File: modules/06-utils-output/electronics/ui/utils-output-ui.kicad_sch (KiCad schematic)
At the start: 33 parts, among them J1 Conn_02x03_Odd_Even, J2 Conn_02x04_Odd_Even, J4 Conn_01x02, J5 Conn_01x06, J6 Conn_02x05_Odd_Even, J7 Conn_02x03_Odd_Even, Q1 2N3904, Q2 2N3906

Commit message: Added Utils BOM
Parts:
- J2: Part URL (none) -> https://mou.sr/4qqxl75; Part no. (none) -> 200-SSW10401TD; Vendor (none) -> Mouser
- J6: Part URL (none) -> https://mou.sr/4lVCZM9; Part no. (none) -> 200-SSW10501TD; Vendor (none) -> Mouser
- J7: Part URL (none) -> https://mou.sr/3GIDVEr; Part no. (none) -> 200-SSW10301TD; Vendor (none) -> Mouser
- Q1: Part URL (none) -> https://mou.sr/4febysZ; Part no. (none) -> 637-2N3904; Vendor (none) -> Mouser
- Q2: Part URL (none) -> https://mou.sr/4a8lju1; Part no. (none) -> 637-2N3906; Vendor (none) -> Mouser
- R1: Part URL (none) -> https://mou.sr/3MWzgkZ; Part no. (none) -> 603-MFR-25FRF52-47K; Vendor (none) -> Mouser
- R2: Part URL (none) -> https://mou.sr/4q072Ei; Part no. (none) -> 603-MFR25SFTF52-4K7; Vendor (none) -> Mouser
- RV_LFO_AMOUNT1: Part no. (none) -> 652-PTV1124425AA203; Vendor (none) -> Mouser
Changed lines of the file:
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@@
 			)
 		)
-		(property "Part URL" ""
+		(property "Part URL" "https://mou.sr/3GIDVEr"
 			(at 245.11 81.28 0)
 			(effects
@@
 			)
 		)
-		(property "Vendor" ""
+		(property "Vendor" "Mouser"
 			(at 245.11 81.28 0)
 			(effects
@@
 			)
 		)
+		(property "Part no." "200-SSW10301TD"
+			(at 245.11 81.28 0)
+			(effects
+				(font
+					(size 1.27 1.27)
+				)
+				(hide yes)
+			)
+		)
 		(pin "3"
 		)
@@
 			)
 		)
-		(property "Vendor" ""
+		(property "Vendor" "Mouser"
 			(at 135.89 55.88 0)
 			(effects
@@
 			)
 		)
+		(property "Part no." "652-PTV1124425AA203 "
+			(at 135.89 55.88 0)
+			(effects
+				(font
+					(size 1.27 1.27)
+				)
+				(hide yes)
+			)
+		)
 		(pin "1"
 		)
@@
 			)
 		)
-		(property "Part URL" ""
+		(property "Part URL" "https://mou.sr/4qqxl75"
 			(at 245.11 60.96 0)
 			(effects
@@
 			)
 		)
-		(property "Vendor" ""
+		(property "Vendor" "Mouser"
 			(at 245.11 60.96 0)
 			(effects
@@
 			)
 		)
+		(property "Part no." "200-SSW10401TD"
+			(at 245.11 60.96 0)
+			(effects
+				(font
+					(size 1.27 1.27)
+				)
+				(hide yes)
+			)
+		)
 		(pin "5"
 		)
@@
 			)
 		)
-		(property "Part URL" ""
+		(property "Part URL" "https://mou.sr/4a8lju1"
 			(at 102.87 179.07 0)
 			(effects
@@
 			)
 		)
-		(property "Vendor" ""
+		(property "Vendor" "Mouser"
 			(at 102.87 179.07 0)
 			(effects
@@
 			)
 		)
+		(property "Part no." "637-2N3906"
+			(at 102.87 179.07 0)
+			(effects
+				(font
+					(size 1.27 1.27)
+				)
+				(hide yes)
+			)
+		)
 		(pin "1"
 		)
@@
 			)
 		)
-		(property "Vendor" ""
+		(property "Vendor" "Mouser"
 			(at 105.41 55.88 0)
 			(effects
@@
 			)
 		)
+		(property "Part no." "652-PTV1124425AA203 "
+			(at 105.41 55.88 0)
+			(effects
+				(font
+					(size 1.27 1.27)
+				)
+				(hide yes)
+			)
+		)
 		(pin "1"
 		)
@@
 			)
 		)
-		(property "Part URL" ""
+		(property "Part URL" "https://mou.sr/4febysZ"
 			(at 102.87 156.21 0)
 			(effects
@@
 			)
 		)
-		(property "Vendor" ""
+		(property "Vendor" "Mouser"
 			(at 102.87 156.21 0)
 			(effects
@@
 			)
 		)
+		(property "Part no." "637-2N3904"
+			(at 102.87 156.21 0)
+			(effects
+				(font
+					(size 1.27 1.27)
+				)
+				(hide yes)
+			)
+		)
 		(pin "2"
 		)
@@
 			)
 		)
-		(property "Part URL" ""
+		(property "Part URL" "https://mou.sr/3MWzgkZ"
 			(at 90.17 156.21 0)
 			(effects
@@
 			)
 		)
-		(property "Vendor" ""
+		(property "Vendor" "Mouser"
 			(at 90.17 156.21 0)
 			(effects
@@
 			)
 		)
+		(property "Part no." "603-MFR-25FRF52-47K"
+			(at 90.17 156.21 90)
+			(effects
+				(font
+					(size 1.27 1.27)
+				)
+				(hide yes)
+			)
+		)
 		(pin "1"
 		)
@@
 			)
 		)
-		(property "Part URL" ""
+		(property "Part URL" "https://mou.sr/4lVCZM9"
 			(at 245.11 100.33 0)
 			(effects
@@
 			)
 		)
-		(property "Vendor" ""
+		(property "Vendor" "Mouser"
 			(at 245.11 100.33 0)
 			(effects
@@
 			)
 		)
+		(property "Part no." "200-SSW10501TD"
+			(at 245.11 100.33 0)
+			(effects
+				(font
+					(size 1.27 1.27)
+				)
+				(hide yes)
+			)
+		)
 		(pin "1"
 		)
@@
 			)
 		)
-		(property "Part URL" ""
+		(property "Part URL" "https://mou.sr/4q072Ei"
 			(at 105.41 146.05 0)
 			(effects
@@
 			)
 		)
-		(property "Vendor" ""
+		(property "Vendor" "Mouser"
 			(at 105.41 146.05 0)
 			(effects
@@
 			(at 105.41 146.05 0)
 			(effects
+				(font
+					(size 1.27 1.27)
+				)
+				(hide yes)
+			)
+		)
+		(property "Part no." "603-MFR25SFTF52-4K7"
+			(at 105.41 146.05 0)
+			(effects

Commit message: Fixed UI component part number bugs
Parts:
- RV_CRUSH1: Part URL https://mou.sr/4694GMU -> https://mou.sr/3VpxrOs; Part no. 652-PTV09A4025FB104 -> 652-PTV09A4025FA105
- RV_LFO_RATE1: value A500k -> A500k-1M; Part URL https://mou.sr/4694GMU -> https://mou.sr/3VpxrOs; Part no. 652-PTV09A4025FB104 -> 652-PTV09A4025FA105
- RV_MAIN_VOLUME1: Part URL https://mou.sr/4694GMU -> https://mou.sr/4bCOV0e; Part no. 652-PTV09A4025FB104 -> 652-PTV09A4025FA103
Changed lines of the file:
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@@
 			)
 		)
-		(property "Part URL" "https://mou.sr/4694GMU"
+		(property "Part URL" "https://mou.sr/4bCOV0e"
 			(at 171.45 29.21 0)
 			(effects
@@
 			)
 		)
-		(property "Part no." "652-PTV09A4025FB104"
+		(property "Part no." "652-PTV09A4025FA103"
 			(at 171.45 29.21 0)
 			(effects
@@
 			)
 		)
-		(property "Part URL" "https://mou.sr/4694GMU"
+		(property "Part URL" "https://mou.sr/3VpxrOs"
 			(at 34.29 29.21 0)
 			(effects
@@
 			)
 		)
-		(property "Part no." "652-PTV09A4025FB104"
+		(property "Part no." "652-PTV09A4025FA105"
 			(at 34.29 29.21 0)
 			(effects
@@
 			)
 		)
-		(property "Value" "A500k"
+		(property "Value" "A500k-1M"
 			(at 102.87 27.9401 0)
 			(effects
@@
 			)
 		)
-		(property "Part URL" "https://mou.sr/4694GMU"
+		(property "Part URL" "https://mou.sr/3VpxrOs"
 			(at 105.41 29.21 0)
 			(effects
@@
 			)
 		)
-		(property "Part no." "652-PTV09A4025FB104"
+		(property "Part no." "652-PTV09A4025FA105"
 			(at 105.41 29.21 0)
 			(effects

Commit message: Updated UI BOMs
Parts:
- RV_CRUSH1, RV_LFO_AMOUNT1, RV_LFO_RATE1, RV_MAIN_VOLUME1: Note (none) -> D-Shaft
- RV_DRIVE1: Note (none) -> Knurled Shaft; Part URL https://mou.sr/4694GMU -> https://mou.sr/41lYe2k; Part no. 652-PTV09A4025FB104 -> 652-PTV09A4025UB104

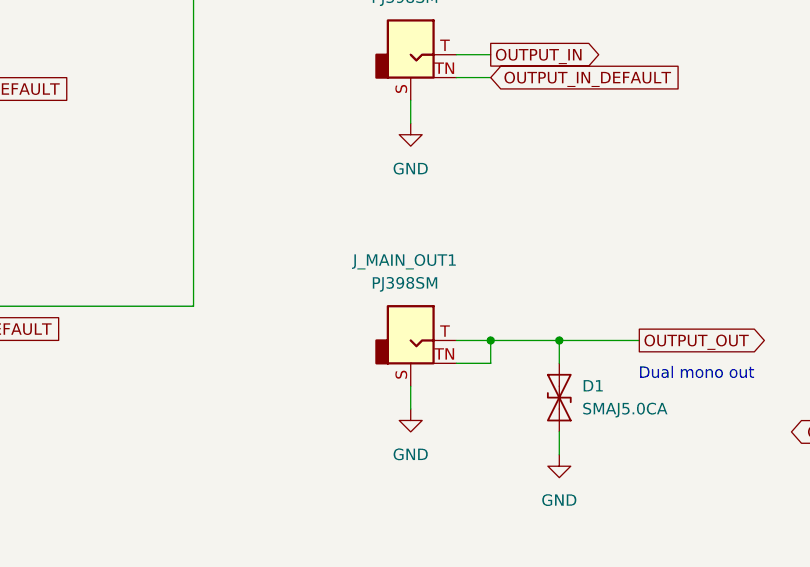
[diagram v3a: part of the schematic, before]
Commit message: Updated main output jack part no
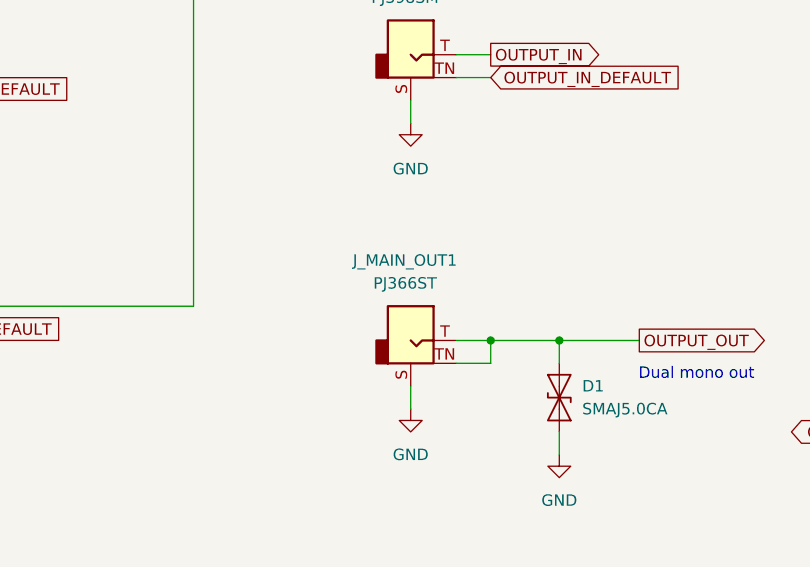
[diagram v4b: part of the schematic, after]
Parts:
- J_MAIN_OUT1: value PJ398SM -> PJ366ST; Note (none) -> Stereo jack; Part URL https://www.thonk.co.uk/shop/thonkiconn/ -> https://www.thonk.co.uk/shop/3-5mm-jacks/; Part no. PJ398SM -> PJ366ST
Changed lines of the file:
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@@
 			)
 		)
-		(property "Value" "PJ398SM"
+		(property "Value" "PJ366ST"
 			(at 170.815 109.22 0)
 			(effects
@@
 			)
 		)
-		(property "Part URL" "https://www.thonk.co.uk/shop/thonkiconn/"
+		(property "Part URL" "https://www.thonk.co.uk/shop/3-5mm-jacks/"
 			(at 171.45 115.57 0)
 			(effects
@@
 			)
 		)
-		(property "Part no." "PJ398SM"
+		(property "Part no." "PJ366ST"
 			(at 171.45 115.57 0)
 			(effects
@@
 			)
 		)
-		(property "Note" ""
+		(property "Note" "Stereo jack"
 			(at 171.45 115.57 0)
 			(effects
+				(font
+					(size 1.27 1.27)
+				)
+				(hide yes)
+			)
+		)
+		(property "Part No." ""
+			(at 171.45 115.57 0)
+			(effects

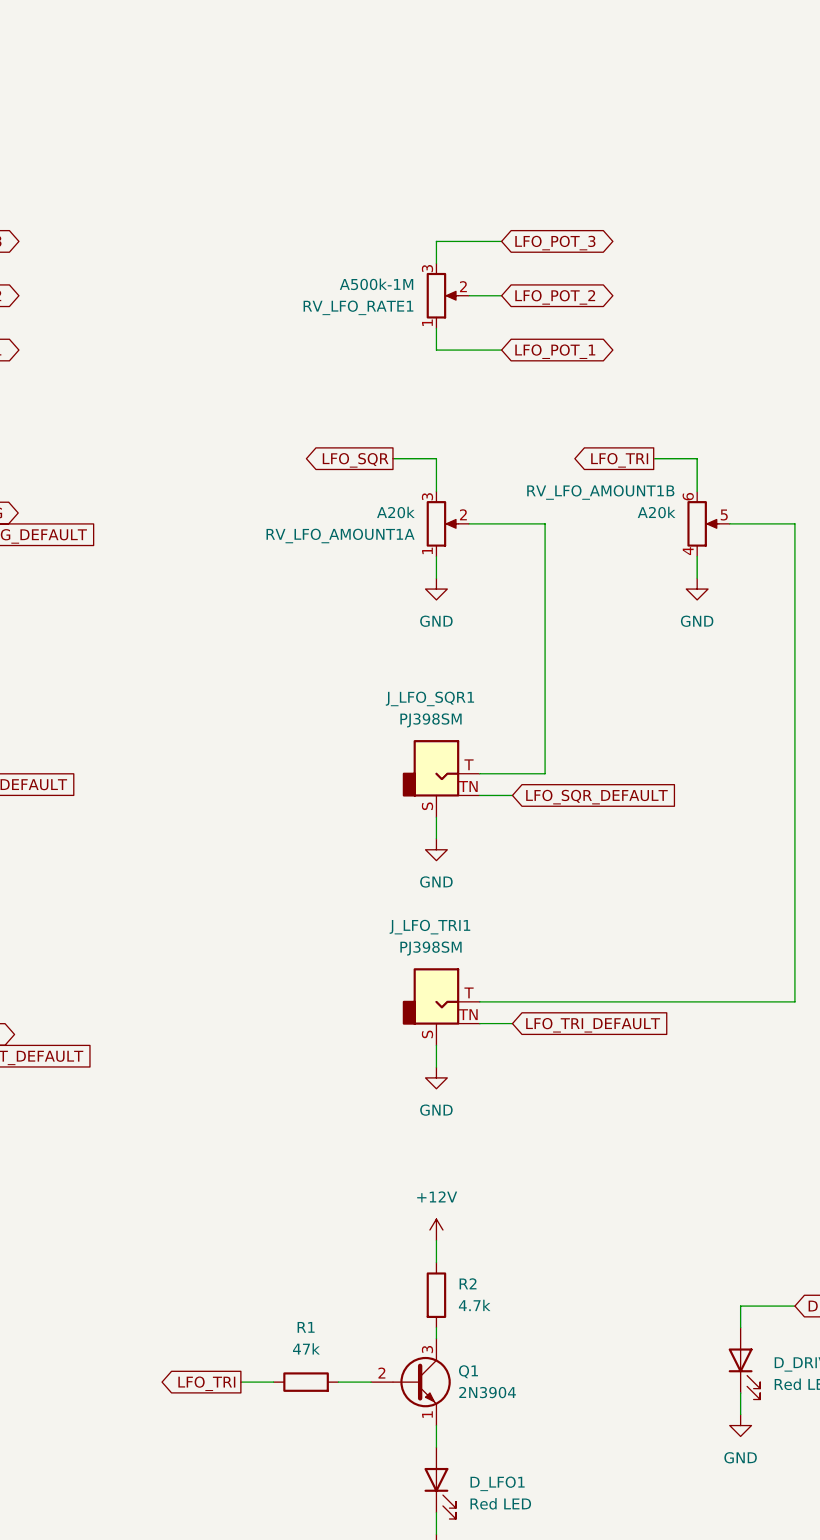
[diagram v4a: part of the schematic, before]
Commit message: Improved LFO LED network
The LFO LED transistor needed a little feedback bias to make it pulse nicely along with the triangle wave.
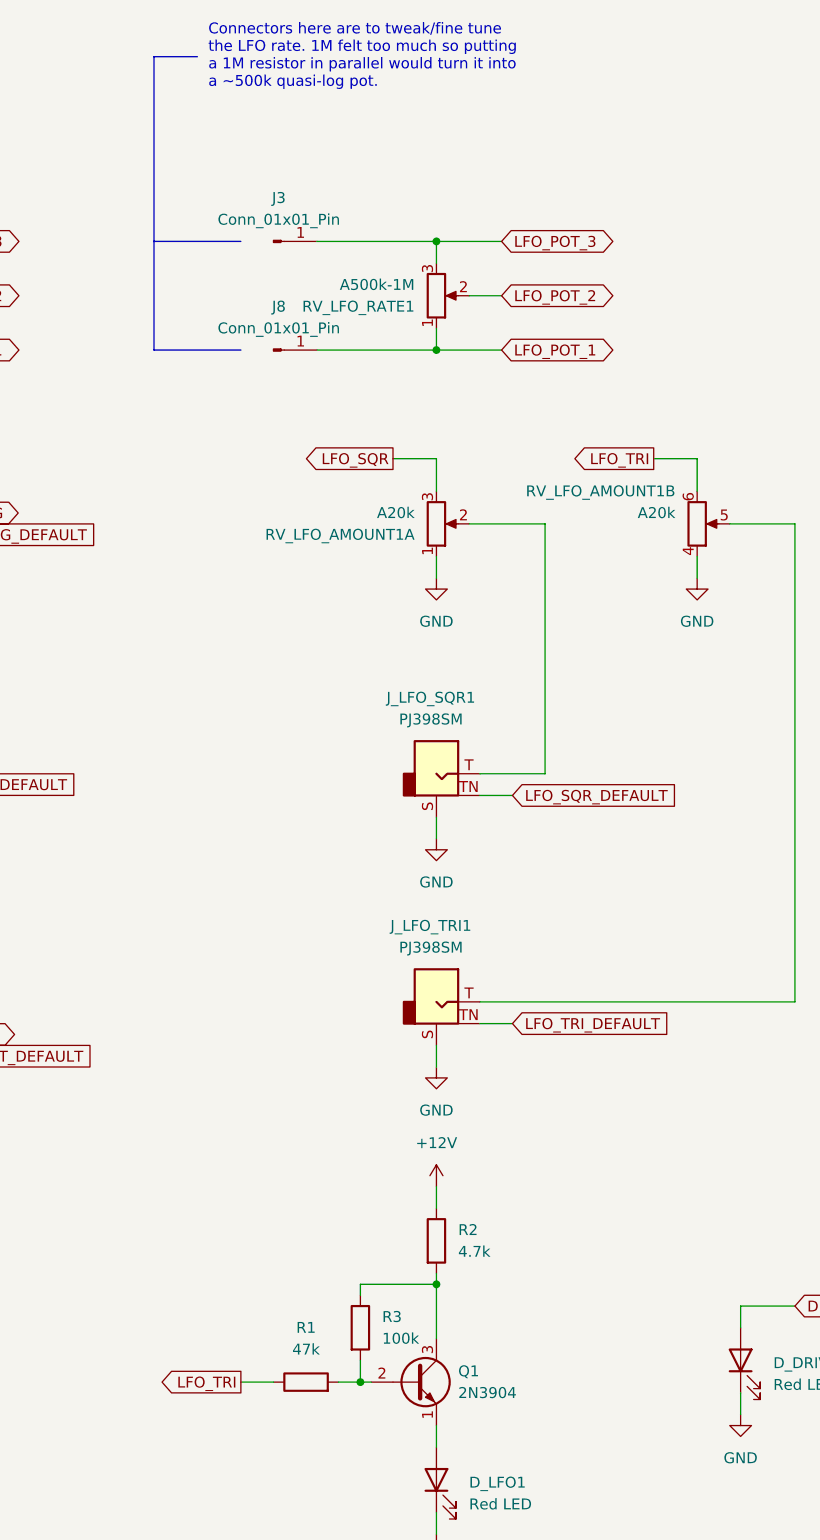
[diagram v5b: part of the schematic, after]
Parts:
- added J3, J8: Conn_01x01_Pin, TestPoint:TestPoint_THTPad_1.5x1.5mm_Drill0.7mm, symbol Connector:Conn_01x01_Pin
- added R3: 100k, Shmoergh_Custom_Footprints:R_Axial_DIN0207_L6.3mm_D2.5mm_P7.62mm_Horizontal, symbol Device:R
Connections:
- net LFO_POT_1: now also J8.1 (Pin_1)
- net LFO_POT_3: now also J3.1 (Pin_1)
- net at Q1.2 (B), R1.2: now also R3.2
- net at Q1.3 (C), R2.2: now also R3.1
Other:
- note added: "Connectors here are to tweak/fine tune the LFO rate. 1M felt too much so putting a 1M resistor in parallel would turn it into a ~500k quasi-log pot."
- moved on the sheet: R2

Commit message: Added protection resistor to pulse out on Brain
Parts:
- J3, J8: footprint TestPoint:TestPoint_THTPad_1.5x1.5mm_Drill0.7mm -> TestPoint:TestPoint_THTPad_D2.0mm_Drill1.0mm
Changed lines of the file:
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@@
 			)
 		)
-		(property "Footprint" "TestPoint:TestPoint_THTPad_1.5x1.5mm_Drill0.7mm"
+		(property "Footprint" "TestPoint:TestPoint_THTPad_D2.0mm_Drill1.0mm"
 			(at 86.36 22.86 0)
 			(effects
@@
 			)
 		)
-		(property "Footprint" "TestPoint:TestPoint_THTPad_1.5x1.5mm_Drill0.7mm"
+		(property "Footprint" "TestPoint:TestPoint_THTPad_D2.0mm_Drill1.0mm"
 			(at 86.36 35.56 0)
 			(effects

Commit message: KiCAD version update - Utils
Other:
- title: Hog Moduleur Sidechain Mixer UI -> Utils + Output UI
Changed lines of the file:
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@@
 	(paper "A4")
 	(title_block
-		(title "Hog Moduleur Sidechain Mixer UI")
-		(date "2025-10-24")
-		(rev "v0.2")
+		(title "Utils + Output UI")
+		(date "2026-02-21")
+		(rev "v1.1")
 		(company "Shmøergh")
 	)
